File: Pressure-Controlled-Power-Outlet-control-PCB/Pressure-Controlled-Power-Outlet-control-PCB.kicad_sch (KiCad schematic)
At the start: 53 parts, among them J1 pressure sensor, J10 Conn_01x02_Pin, J2 1017514, J3 I2C0 Connector, J4 SPI1 Connector, J5 FanA 5V/12V, J6 FanB 5V/12V, J7 Conn_01x02_Pin, K1 T9GV5L24-24, K2 T9GV5L24-24, M1 Fan_4pin, M2 Fan_4pin, Q1 2N3906, Q2 IRF540N, Q3 IRF540N, Q4 2N3906, Q5 2N3904, Q6 2N3904, Q7 2N3904, Q8 2N3904, U1 Pico, U2 LM324, U3 LD1085V50, U4 LM1085-12

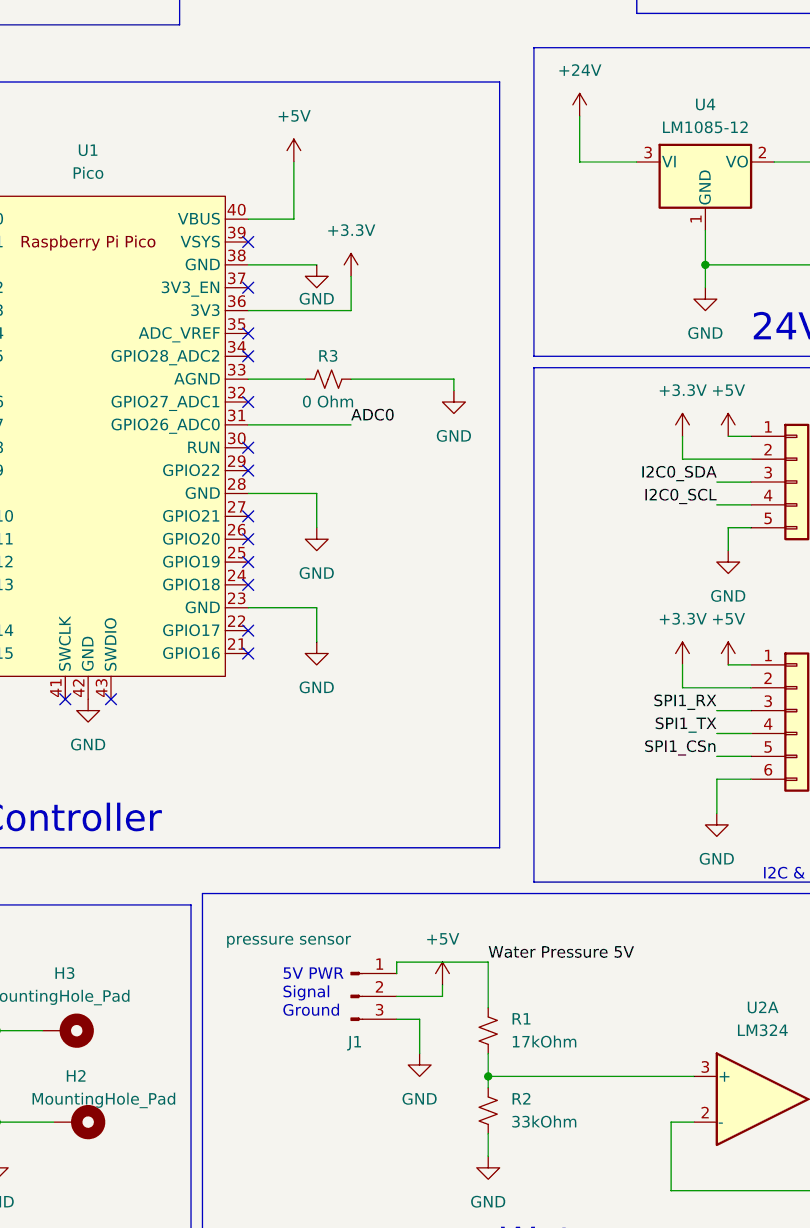
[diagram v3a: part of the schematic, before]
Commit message: added some power filter caps
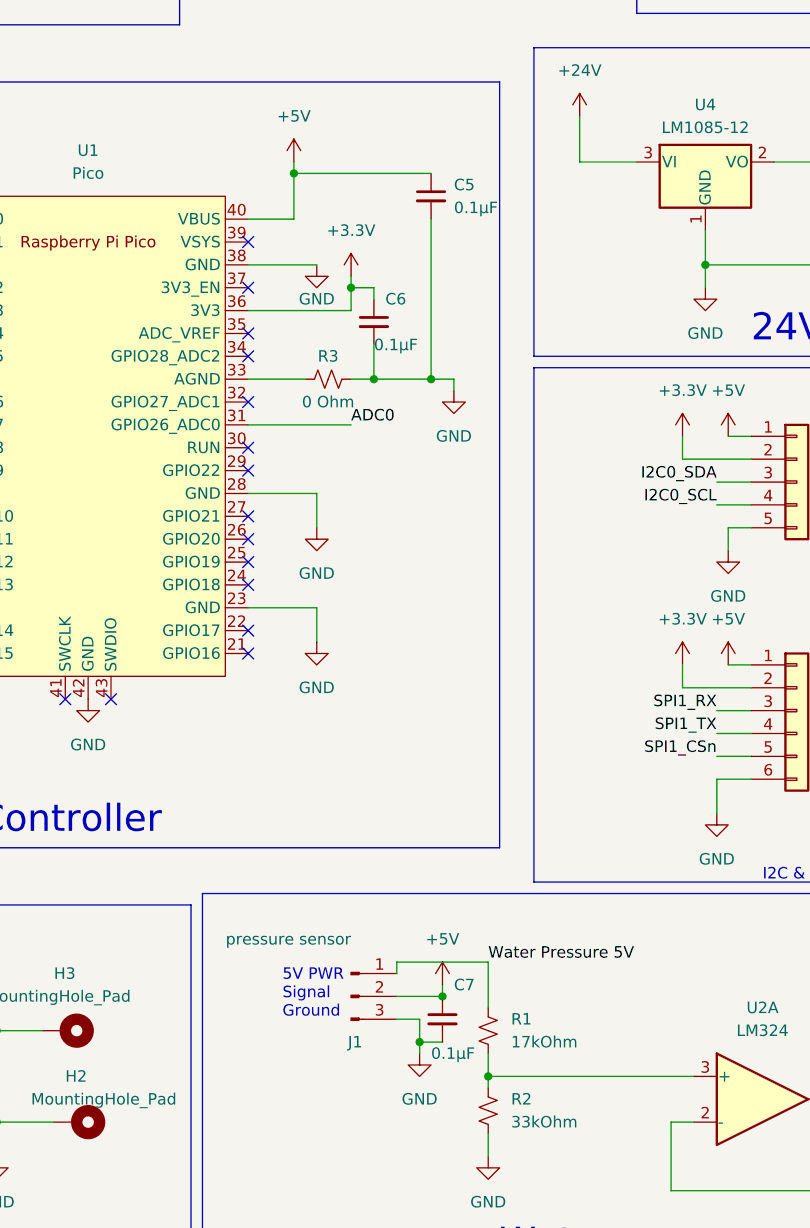
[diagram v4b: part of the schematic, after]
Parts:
- added C5, C6, C7: 0.1µF, Capacitor_THT:C_Rect_L7.2mm_W2.5mm_P5.00mm_FKS2_FKP2_MKS2_MKP2, symbol Device:C_Small
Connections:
- net +3.3V: now also C6.1
- net +5V: now also C5.1, C7.1
- net GND: now also C5.2, C6.2, C7.2
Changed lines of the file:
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@@
   (junction (at 157.48 49.53) (diameter 0) (color 0 0 0 0)
   )
+  (junction (at 80.01 88.9) (diameter 0) (color 0 0 0 0)
+  )
   (junction (at 228.6 125.73) (diameter 0) (color 0 0 0 0)
   )
+  (junction (at 73.66 76.2) (diameter 0) (color 0 0 0 0)
+  )
   (junction (at 157.48 39.37) (diameter 0) (color 0 0 0 0)
   )
   (junction (at 204.47 114.3) (diameter 0) (color 0 0 0 0)
   )
+  (junction (at 87.63 172.72) (diameter 0) (color 0 0 0 0)
+  )
+  (junction (at 90.17 167.64) (diameter 0) (color 0 0 0 0)
+  )
   (junction (at 48.26 49.53) (diameter 0) (color 0 0 0 0)
   )
   (junction (at 243.84 93.98) (diameter 0) (color 0 0 0 0)
   )
+  (junction (at 82.55 99.06) (diameter 0) (color 0 0 0 0)
+  )
   (junction (at 40.64 181.61) (diameter 0) (color 0 0 0 0)
   )
@@
   )
   (junction (at 232.41 115.57) (diameter 0) (color 0 0 0 0)
+  )
+  (junction (at 88.9 99.06) (diameter 0) (color 0 0 0 0)
   )
   (junction (at 99.06 30.48) (diameter 0) (color 0 0 0 0)
@@
     (stroke (width 0) (type default))
   )
+  (wire (pts (xy 82.55 95.25) (xy 82.55 99.06))
+    (stroke (width 0) (type default))
+  )
   (wire (pts (xy 274.32 24.13) (xy 274.32 25.4))
     (stroke (width 0) (type default))
@@
     (stroke (width 0) (type default))
   )
+  (wire (pts (xy 82.55 88.9) (xy 80.01 88.9))
+    (stroke (width 0) (type default))
+  )
   (wire (pts (xy 170.18 134.62) (xy 173.99 134.62))
     (stroke (width 0) (type default))
@@
     (stroke (width 0) (type default))
   )
+  (wire (pts (xy 88.9 99.06) (xy 91.44 99.06))
+    (stroke (width 0) (type default))
+  )
   (wire (pts (xy 76.2 128.27) (xy 76.2 124.46))
     (stroke (width 0) (type default))
@@
     (stroke (width 0) (type default))
   )
+  (wire (pts (xy 88.9 81.28) (xy 88.9 99.06))
+    (stroke (width 0) (type default))
+  )
   (wire (pts (xy 99.06 40.64) (xy 85.09 40.64))
     (stroke (width 0) (type default))
@@
     (stroke (width 0) (type default))
   )
-  (wire (pts (xy 80.01 99.06) (xy 91.44 99.06))
+  (wire (pts (xy 80.01 99.06) (xy 82.55 99.06))
     (stroke (width 0) (type default))
   )
@@
     (stroke (width 0) (type default))
   )
-  (wire (pts (xy 87.63 173.99) (xy 87.63 170.18))
+  (wire (pts (xy 87.63 173.99) (xy 87.63 172.72))
     (stroke (width 0) (type default))
   )
@@
     (stroke (width 0) (type default))
   )
+  (wire (pts (xy 82.55 90.17) (xy 82.55 88.9))
+    (stroke (width 0) (type default))
+  )
   (wire (pts (xy 204.47 114.3) (xy 209.55 114.3))
     (stroke (width 0) (type default))
@@
     (stroke (width 0) (type default))
   )
+  (wire (pts (xy 87.63 172.72) (xy 90.17 172.72))
+    (stroke (width 0) (type default))
+  )
   (wire (pts (xy 214.63 20.32) (xy 214.63 25.4))
     (stroke (width 0) (type default))
@@
     (stroke (width 0) (type default))
   )
-  (wire (pts (xy 80.01 91.44) (xy 80.01 87.63))
+  (wire (pts (xy 80.01 91.44) (xy 80.01 88.9))
     (stroke (width 0) (type default))
   )
@@
     (stroke (width 0) (type default))
   )
-  (wire (pts (xy 73.66 74.93) (xy 73.66 81.28))
+  (wire (pts (xy 73.66 74.93) (xy 73.66 76.2))
     (stroke (width 0) (type default))
   )
@@
     (stroke (width 0) (type default))
   )
+  (wire (pts (xy 73.66 76.2) (xy 88.9 76.2))
+    (stroke (width 0) (type default))
+  )
   (wire (pts (xy 95.25 163.83) (xy 95.25 168.91))
     (stroke (width 0) (type default))
@@
     (stroke (width 0) (type default))
   )
+  (wire (pts (xy 82.55 99.06) (xy 88.9 99.06))
+    (stroke (width 0) (type default))
+  )
   (wire (pts (xy 19.05 124.46) (xy 33.02 124.46))
     (stroke (width 0) (type default))
@@
     (stroke (width 0) (type default))
   )
+  (wire (pts (xy 80.01 88.9) (xy 80.01 87.63))
+    (stroke (width 0) (type default))
+  )
+  (wire (pts (xy 73.66 76.2) (xy 73.66 81.28))
+    (stroke (width 0) (type default))
+  )
   (wire (pts (xy 243.84 93.98) (xy 243.84 90.17))
     (stroke (width 0) (type default))
@@
   )
   (wire (pts (xy 237.49 36.83) (xy 233.68 36.83))
+    (stroke (width 0) (type default))
+  )
+  (wire (pts (xy 87.63 172.72) (xy 87.63 170.18))
     (stroke (width 0) (type default))
   )
@@
         (path "/db34d92e-5e84-4492-8b7e-15d9a09f9218"
           (reference "R15") (unit 1)
+        )
+      )
+    )
+  )
+  (symbol (lib_id "Device:C_Small") (at 82.55 92.71 0) (unit 1)
+    (in_bom yes) (on_board yes) (dnp no)
+    (property "Reference" "C6" (at 83.82 90.17 0)
+      (effects (font (size 1.27 1.27)) (justify left))
+    )
+    (property "Value" "0.1µF" (at 82.55 95.25 0)
+      (effects (font (size 1.27 1.27)) (justify left))
+    )
+    (property "Footprint" "Capacitor_THT:C_Rect_L7.2mm_W2.5mm_P5.00mm_FKS2_FKP2_MKS2_MKP2" (at 82.55 92.71 0)
+      (effects (font (size 1.27 1.27)) hide)
+    )
+    (property "Datasheet" "~" (at 82.55 92.71 0)
+      (effects (font (size 1.27 1.27)) hide)
+    )
+    (pin "1")
+    (pin "2")
+    (instances
+      (project "Pressure-Controlled-Power-Outlet-control-PCB"
+        (path "/db34d92e-5e84-4492-8b7e-15d9a09f9218"
+          (reference "C6") (unit 1)
         )
       )
@@
     )
   )
+  (symbol (lib_id "Device:C_Small") (at 90.17 170.18 0) (unit 1)
+    (in_bom yes) (on_board yes) (dnp no)
+    (property "Reference" "C7" (at 91.44 166.37 0)
+      (effects (font (size 1.27 1.27)) (justify left))
+    )
+    (property "Value" "0.1µF" (at 88.9 173.99 0)
+      (effects (font (size 1.27 1.27)) (justify left))
+    )
+    (property "Footprint" "Capacitor_THT:C_Rect_L7.2mm_W2.5mm_P5.00mm_FKS2_FKP2_MKS2_MKP2" (at 90.17 170.18 0)
+      (effects (font (size 1.27 1.27)) hide)
+    )
+    (property "Datasheet" "~" (at 90.17 170.18 0)
+      (effects (font (size 1.27 1.27)) hide)
+    )
+    (pin "1")
+    (pin "2")
+    (instances
+      (project "Pressure-Controlled-Power-Outlet-control-PCB"
+        (path "/db34d92e-5e84-4492-8b7e-15d9a09f9218"
+          (reference "C7") (unit 1)
+        )
+      )
+    )
+  )
   (symbol (lib_id "Connector_Generic:Conn_01x06") (at 129.54 135.89 0) (unit 1)
     (in_bom yes) (on_board yes) (dnp no) (fields_autoplaced)
@@
         )
       )
+    )
+  )
+  (symbol (lib_id "Device:C_Small") (at 88.9 78.74 0) (unit 1)
+    (in_bom yes) (on_board yes) (dnp no) (fields_autoplaced)
+    (property "Reference" "C5" (at 91.44 77.4763 0)
+      (effects (font (size 1.27 1.27)) (justify left))
+    )
+    (property "Value" "0.1µF" (at 91.44 80.0163 0)
+      (effects (font (size 1.27 1.27)) (justify left))
+    )
+    (property "Footprint" "Capacitor_THT:C_Rect_L7.2mm_W2.5mm_P5.00mm_FKS2_FKP2_MKS2_MKP2" (at 88.9 78.74 0)
+      (effects (font (size 1.27 1.27)) hide)
+    )
+    (property "Datasheet" "~" (at 88.9 78.74 0)
+      (effects (font (size 1.27 1.27)) hide)
+    )
+    (pin "1")
+    (pin "2")
+    (instances
+      (project "Pressure-Controlled-Power-Outlet-control-PCB"
+        (path "/db34d92e-5e84-4492-8b7e-15d9a09f9218"
+          (reference "C5") (unit 1)
+        )
+      )
